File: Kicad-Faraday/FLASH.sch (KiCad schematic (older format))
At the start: 3 parts, among them U9 IS25LQ080-JNLE-TR

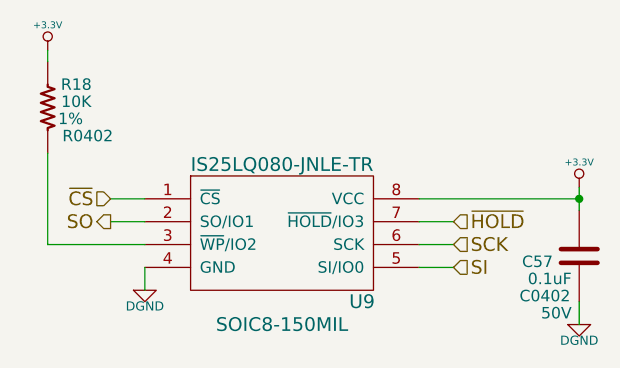
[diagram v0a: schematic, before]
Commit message: Removed basic parts I don't really need to test or am so confident that testing will be fine I'm OK making the changes well in advance
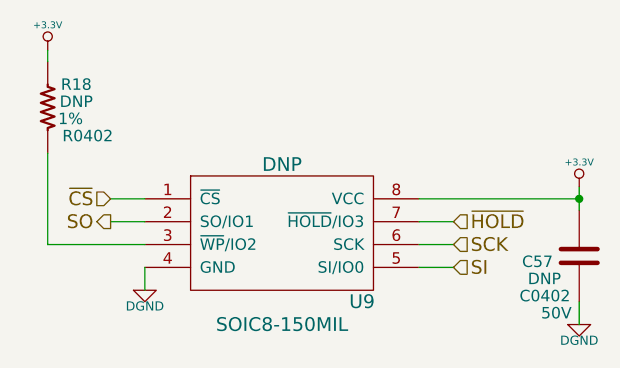
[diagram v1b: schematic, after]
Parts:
- C46: value 0.1uF -> DNP
- R18: value 10K -> DNP
- U9: value IS25LQ080-JNLE-TR -> DNP
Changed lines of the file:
@@
 Sheet 6 11
 Title "Faraday Wireless Node"
-Date "24 oct 2016"
+Date "2 nov 2016"
 Rev "C"
 Comp "FaradayRF"
@@
 P 9600 4950
 AR Path="/55DC4A3F/578C356D" Ref="#PWR064"  Part="1"
-AR Path="/578A1737/578C356D" Ref="#PWR062"  Part="1"
-F 0 "#PWR062" H 9600 4910 30  0001 C CNN
+AR Path="/578A1737/578C356D" Ref="#PWR061"  Part="1"
+F 0 "#PWR061" H 9600 4910 30  0001 C CNN
 F 1 "+3.3V" H 9600 5060 30  0000 C CNN
 F 2 "" H 9600 4950 60  0000 C CNN
@@
 AR Path="/578A1737/578C356E" Ref="C57"  Part="1"
 F 0 "C57" H 9350 5225 50  0000 L CNN
-F 1 "0.1uF" H 9375 5150 50  0000 L CNN
+F 1 "DNP" H 9375 5150 50  0000 L CNN
 F 2 "C0402" H 9450 5075 50  0000 C CNN
 F 3 "" H 9600 5250 60  0000 C CNN
@@
 P 9600 5550
 AR Path="/55DC4A3F/578C356F" Ref="#PWR065"  Part="1"
-AR Path="/578A1737/578C356F" Ref="#PWR063"  Part="1"
-F 0 "#PWR063" H 9600 5550 40  0001 C CNN
+AR Path="/578A1737/578C356F" Ref="#PWR062"  Part="1"
+F 0 "#PWR062" H 9600 5550 40  0001 C CNN
 F 1 "DGND" H 9600 5480 40  0000 C CNN
 F 2 "~" H 9600 5550 60  0000 C CNN
@@
 P 7700 5400
 AR Path="/55DC4A3F/55DC59F6" Ref="#PWR066"  Part="1"
-AR Path="/578A1737/55DC59F6" Ref="#PWR064"  Part="1"
-F 0 "#PWR064" H 7700 5400 40  0001 C CNN
+AR Path="/578A1737/55DC59F6" Ref="#PWR063"  Part="1"
+F 0 "#PWR063" H 7700 5400 40  0001 C CNN
 F 1 "DGND" H 7700 5330 40  0000 C CNN
 F 2 "~" H 7700 5400 60  0000 C CNN
@@
 P 8300 5150
 F 0 "U9" H 8650 4850 60  0000 C CNN
-F 1 "IS25LQ080-JNLE-TR" H 8300 5450 60  0000 C CNN
+F 1 "DNP" H 8300 5450 60  0000 C CNN
 F 2 "SOIC8-150MIL" H 8300 4750 60  0000 C CNN
 F 3 "~" H 8300 5150 60  0000 C CNN
@@
 $EndComp
 $Comp
-L +3.3V #PWR065
+L +3.3V #PWR064
 U 1 1 578C7130
 P 7275 4350
-F 0 "#PWR065" H 7275 4310 30  0001 C CNN
+F 0 "#PWR064" H 7275 4310 30  0001 C CNN
 F 1 "+3.3V" H 7275 4460 30  0000 C CNN
 F 2 "" H 7275 4350 60  0000 C CNN
@@
 P 7275 4600
 F 0 "R18" H 7150 4500 50  0000 C CNN
-F 1 "10K" H 7150 4575 50  0000 C CNN
+F 1 "DNP" H 7150 4575 50  0000 C CNN
 F 2 "R0402" H 7100 4725 50  0000 C CNN
 F 3 "" H 7275 4600 60  0000 C CNN
